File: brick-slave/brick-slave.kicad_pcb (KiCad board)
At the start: 2 copper layers, 61 x 72.4 mm, 4 parts, among them J1 Conn_01x06_Male, J2 Conn_01x06_Male, J3 Conn_01x06_Female, J4 Conn_01x06_Female

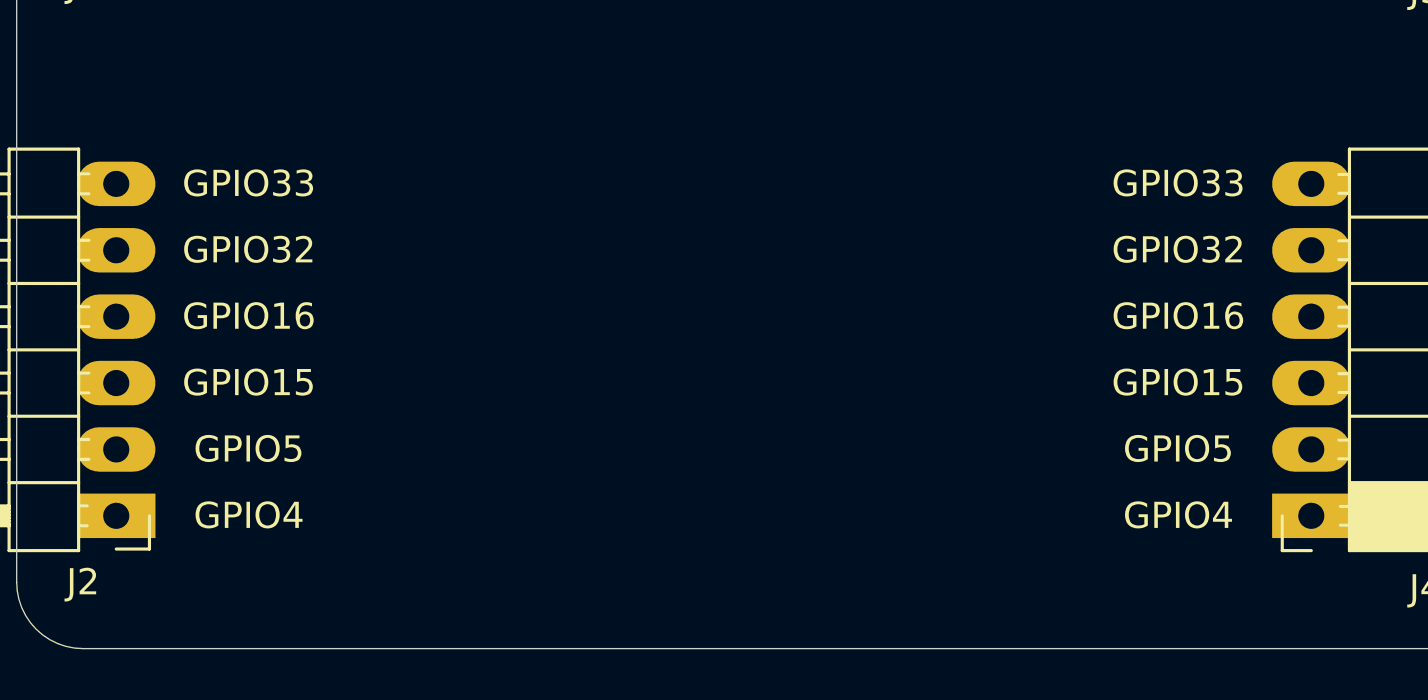
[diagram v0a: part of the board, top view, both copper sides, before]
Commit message: update brick-slave template
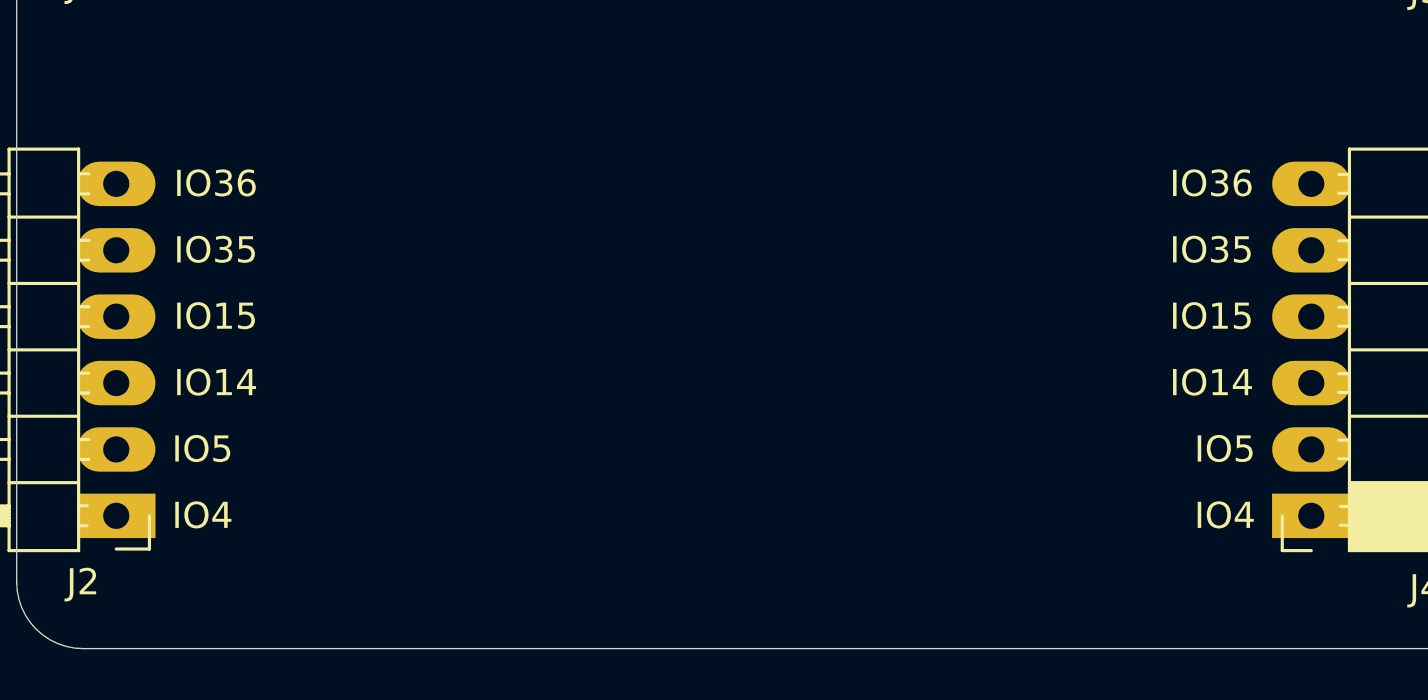
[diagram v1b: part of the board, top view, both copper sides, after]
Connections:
- net GPIO32 renamed GPIO35
- net GPIO33 renamed GPIO36
- J2 pad 3: GPIO15 -> GPIO14
- J2 pad 4: GPIO16 -> GPIO15
- J4 pad 3: GPIO15 -> GPIO14
- J4 pad 4: GPIO16 -> GPIO15
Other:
- board text added: "IO14"
- board text added: "IO15"
- board text added: "IO35"
- board text added: "IO36"
- board text added: "IO4"
- board text added: "IO5"
- board text removed: "GPIO15"
- board text removed: "GPIO16"
- board text removed: "GPIO32"
- board text removed: "GPIO33"
- board text removed: "GPIO4"
- board text removed: "GPIO5"

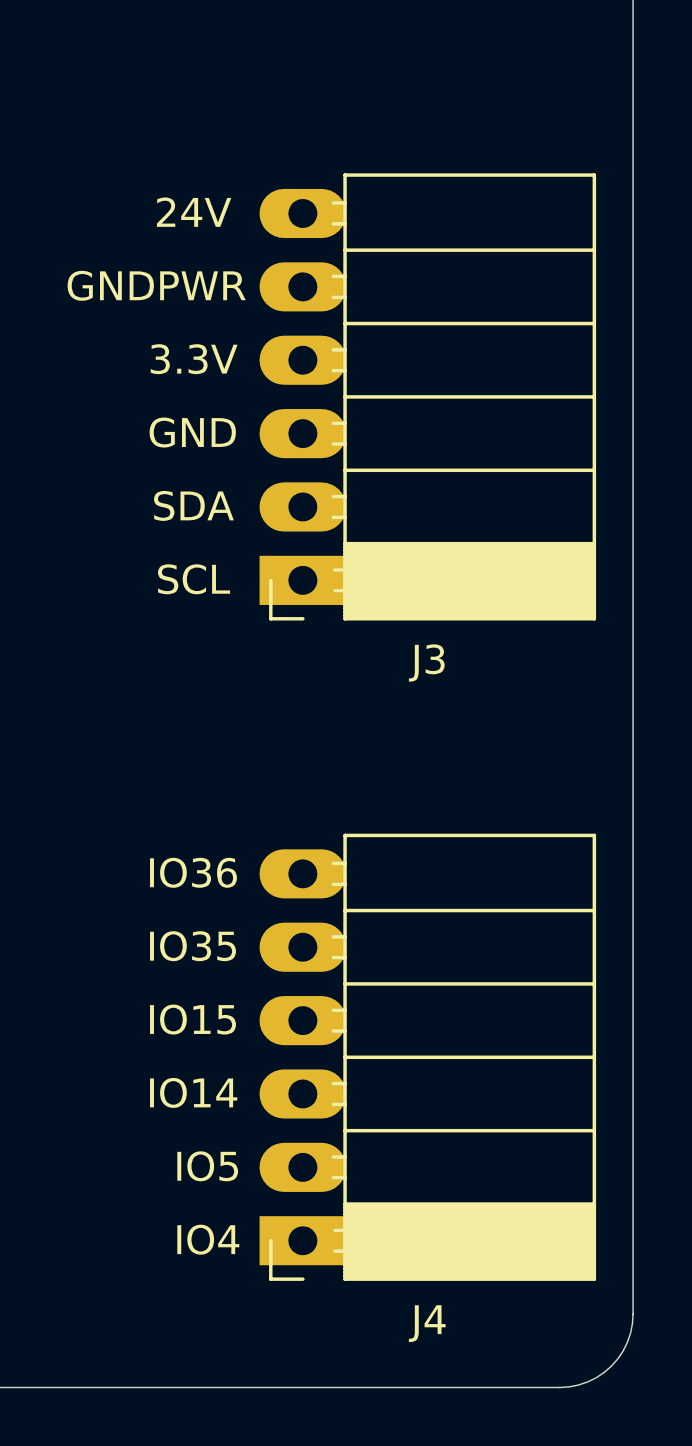
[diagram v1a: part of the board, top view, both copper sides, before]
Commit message: brick-slave - move female connector
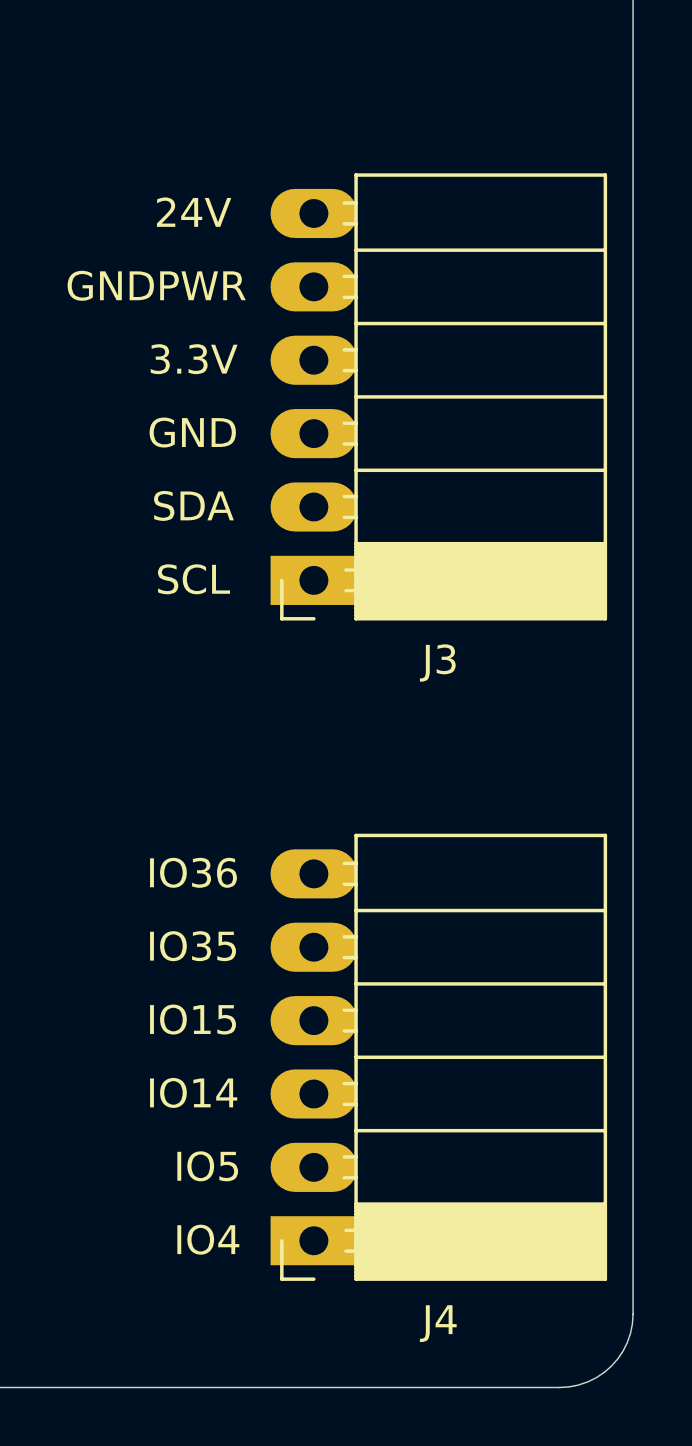
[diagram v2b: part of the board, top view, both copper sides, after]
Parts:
- moved J3 0.38 mm to (113.4, 99.1)
- moved J4 0.38 mm to (113.4, 121.9)

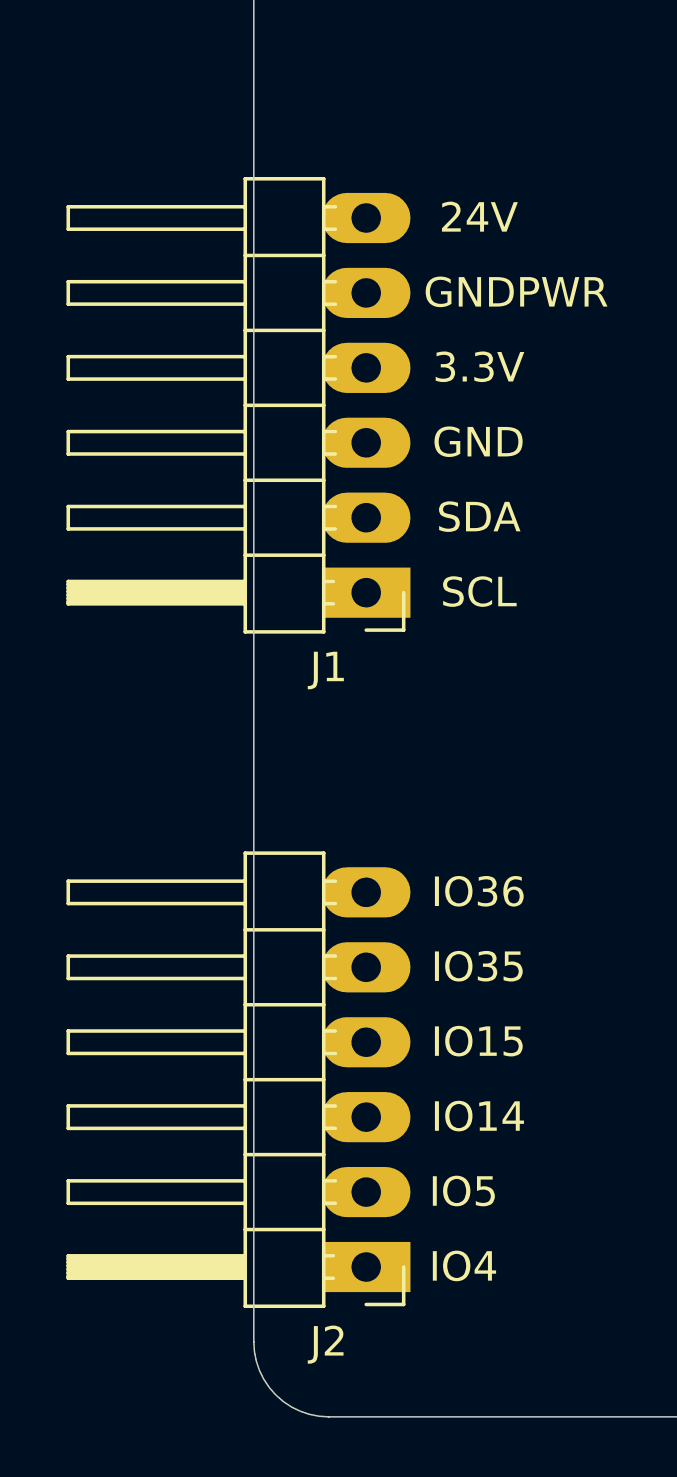
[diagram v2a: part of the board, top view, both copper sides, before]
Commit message: brick-slave - move input connectors
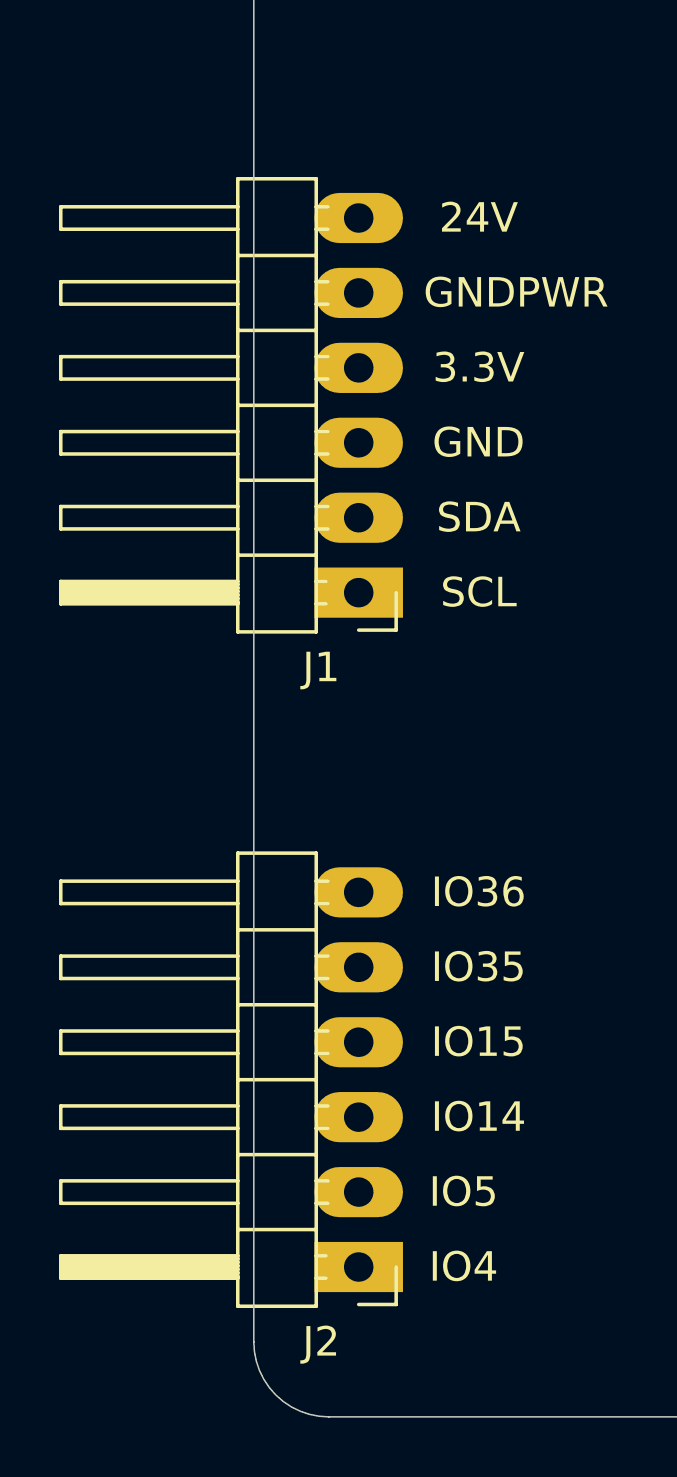
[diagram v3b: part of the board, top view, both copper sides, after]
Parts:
- moved J1 0.25 mm to (67.1, 99.1)
- moved J2 0.25 mm to (67.1, 121.9)

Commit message: upgrade format
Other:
- net class Default removed
- net class Power removed

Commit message: update brick-slave
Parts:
- moved J3 8.64 mm to (104.8, 99.1)
- moved J4 8.64 mm to (104.8, 121.9)
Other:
- board size 61 x 72.4 mm -> 52.3 x 72.4 mm
